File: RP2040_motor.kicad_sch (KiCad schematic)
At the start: 162 parts, among them J1 USB_C_Receptacle_USB2.0, J2 Conn_01x05, J3 Conn_01x06, J4 Conn_01x04, J5 Conn_01x04, J6 Conn_01x03, SW1 SW_MEC_5G, U1 EG2131, U10 EG2131, U11 RP2040, U2 EG2131, U3 LM358, U4 EG2131, U5 EG2131, U6 XL7045, U7 NCP1117-3.3_SOT223, U8 EG2131, U9 W25Q128JVS, Y1 Crystal_GND24

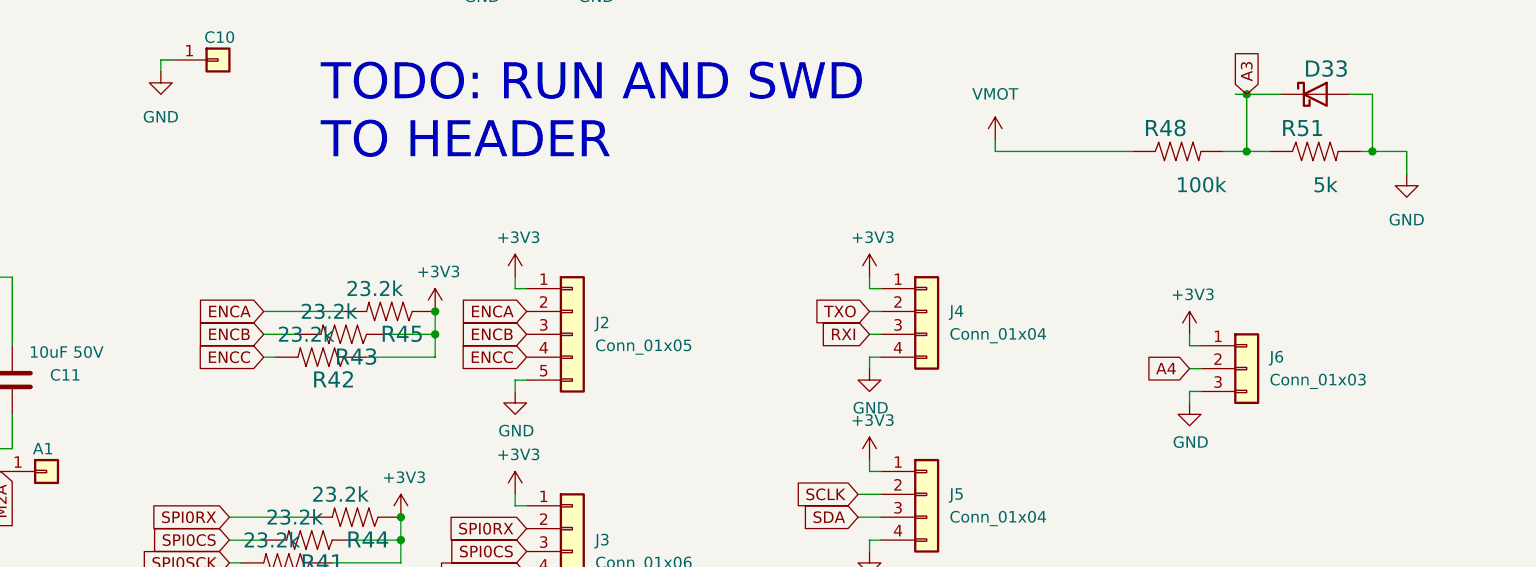
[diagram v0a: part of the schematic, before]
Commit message: Update files for price quote. DO NOT ORDER THESE BOARDS FROM THIS COMMIT!
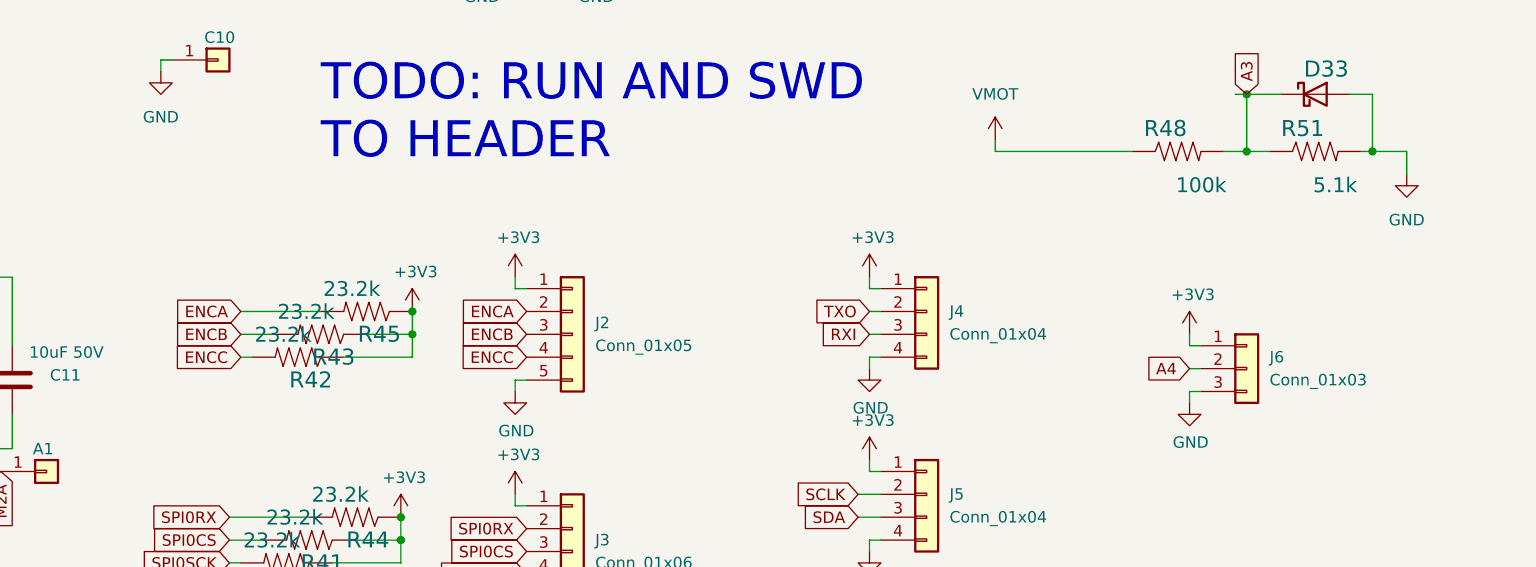
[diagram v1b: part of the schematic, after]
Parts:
- A1, A2, B1, B2, C10, C18, C5, C9: now left out of the parts list
- AH1, AH2, AL1, AL2, BH1, BH2, BL1, BL2, CH1, CH2, CL1, CL2: JLCPCB C180959 -> (none); LCSC (none) -> C180959
- C$1: JLCPCB C28233 -> (none); LCSC (none) -> C28233
- C$2: JLCPCB C440196 -> (none); LCSC (none) -> C440196
- C1, C12, C21, C25, C26, C29, C30, C32, C34, C35, C36, C37, C38, C39, C6, C8, R10, R31, R37: JLCPCB C14663 -> (none); LCSC (none) -> C14663
- C11, C17, C24, C28, C4, C7: JLCPCB C440198 -> (none); LCSC (none) -> C440198
- C13, C14, C15, C2, C3: JLCPCB C72524 -> (none); LCSC (none) -> C72524
- C16, C20, C27: JLCPCB C15850 -> (none); LCSC (none) -> C15850
- C19: JLCPCB C267470 -> (none); LCSC (none) -> C267470
- C22, C23: JLCPCB C1648 -> (none); LCSC (none) -> C1648
- C31, C33: JLCPCB C15849 -> (none); LCSC (none) -> C15849
- D1, D11, D16, D23, D28, D6: JLCPCB C511885 -> (none); LCSC (none) -> C511885
- D10, D14, D15, D19, D20, D21, D26, D27, D31, D32, D4, D5, D9: JLCPCB C8598 -> (none); LCSC (none) -> C8598
- D12, D13, D17, D18, D2, D24, D25, D29, D3, D30, D7, D8: JLCPCB C2128 -> (none); LCSC (none) -> C2128
- D22: JLCPCB C14996 -> (none); LCSC (none) -> C14996
- J1: JLCPCB C2835315 -> (none); LCSC (none) -> C2835315
- J2: JLCPCB C45012 -> (none); LCSC (none) -> C45012
- J3: JLCPCB C140771 -> (none); LCSC (none) -> C140771
- J4, J5: JLCPCB C402777 -> (none); LCSC (none) -> C402777
- J6: LCSC (none) -> C29275
- L1: JLCPCB C49622 -> (none); LCSC (none) -> C49622
- R1, R14, R15, R18, R19, R2, R28, R29, R38, R39, R7, R8: JLCPCB C23345 -> (none); LCSC (none) -> C23345
- R11, R33: JLCPCB C25977 -> (none); LCSC (none) -> C25977
- R12, R34: JLCPCB C403385 -> (none); LCSC (none) -> C403385
- R16, R17, R49, R50: JLCPCB C23186 -> (none); LCSC (none) -> C23186
- R20, R22, R24, R26, R3, R4, R5, R6: JLCPCB C469375 -> (none); LCSC (none) -> C469375
- R21: JLCPCB C37936 -> (none); LCSC (none) -> C37936
- R23: JLCPCB C13167 -> (none); LCSC (none) -> C13167
- R25, R40, R41, R42, R43, R44, R45: JLCPCB C23346 -> (none); LCSC (none) -> C23346
- R27, R30, R35, R9: JLCPCB C22764 -> (none); LCSC (none) -> C22764
- R46, R47: JLCPCB C25190 -> (none); LCSC (none) -> C25190
- R48: LCSC (none) -> C25803
- R51: value 5k -> 5.1k; LCSC (none) -> C23186
- SW1: JLCPCB C13828 -> (none); LCSC (none) -> C13828
- U$1: JLCPCB C21117 -> (none); LCSC (none) -> C21117
- U1, U10, U2, U4, U5, U8: JLCPCB C193777 -> (none); LCSC (none) -> C193777
- U11: JLCPCB C2040 -> (none); LCSC (none) -> C2040
- U3: LCSC (none) -> C7950
- U6: JLCPCB C126474 -> (none); LCSC (none) -> C126474
- U7: JLCPCB C6186 -> (none); LCSC (none) -> C6186
- U9: JLCPCB C97521 -> (none); LCSC (none) -> C97521
- Y1: JLCPCB C9002 -> (none); LCSC (none) -> C9002
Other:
- moved on the sheet: R42, R43, R45

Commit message: In progress independent phase current measurement.
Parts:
- removed R36: DNS, Resistor_SMD:R_0603_1608Metric, symbol MotorController:TAYLOR_RESISTOR
- added C40: 1u, Capacitor_SMD:C_0603_1608Metric, symbol Device:C
- added R36, R55, R58, R59: 0.1uF, Capacitor_SMD:C_0603_1608Metric, symbol MotorController:SPARKFUN-CAPACITORS_CAP
- added R52, R56: 4.64k, Resistor_SMD:R_0603_1608Metric, symbol MotorController:TAYLOR_RESISTOR
- added R53, R57: 133k, Resistor_SMD:R_0603_1608Metric, symbol MotorController:TAYLOR_RESISTOR
- added R54: 499R, Resistor_SMD:R_0603_1608Metric, symbol MotorController:TAYLOR_RESISTOR
- added U12: LM358, Package_SO:MSOP-8_3x3mm_P0.65mm, symbol Amplifier_Operational:LM358
- added U13: ADC081S021CISD/NOPB, ADC081S021:ADC081S021CISD&slash_NOPB, symbol 2022-06-16_01-48-54:ADC081S021CISD/NOPB
- R11, R33: value 6.04k -> 4.64k; LCSC C25977 -> C144652
- R12, R34: value 88.7K -> 133k; LCSC C403385 -> C423080
- R13: value DNS -> 499R; LCSC (none) -> C101076
- R20, R22, R24, R26, R3, R4, R5, R6: value 8mΩ -> 4mΩ; LCSC C469375 -> C375693
- R30, R9: value 1.1k -> 499R; LCSC C22764 -> C101076
- R31, R37: LCSC C14663 -> (none)
- U3: footprint Package_SO:SOIC-8_3.9x4.9mm_P1.27mm -> Package_SO:MSOP-8_3x3mm_P0.65mm; LCSC C7950 -> C54867
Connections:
- net GPIO23 is gone; now on net ENCC: U11.35 (GPIO23)
- net +3V3: now also C40.2, R58.1, R59.1, U12.8 (V+), U13.1 (VA); no longer J6.1 (Pin_1)
- net A1: now also R57.1, U12.1; no longer R34.1, U3.1
- net A2: now also R53.1, U12.7; no longer R12.1, R13.2, U3.7
- net A3: now also R34.1, U3.1; no longer D33.1 (K), R48.2, R51.1
- net A4: now also R12.1, U3.7; no longer J6.2 (Pin_2)
- net ENCC: no longer U11.34 (GPIO22)
- net GND: now also AL1.1 (S), CL2.1 (S), D15.2 (A), D21.2 (A), C40.1, R36.2, R52.2, R55.2, R56.2, R58.2, R59.2, U12.4 (V-), U13.2 (GND); no longer J6.3 (Pin_3), R13.1
- net RUN: now also J6.1 (Pin_1)
- net SWCLK: now also J6.2 (Pin_2)
- net SWD: now also J6.3 (Pin_3)
- net at R33.1, U3.2 (-): no longer R34.2
- net at R10.1, R9.2, U3.5 (+): now also R12.2
- net at R11.1, U3.6 (-): no longer R12.2
- net at R30.2, R31.1, U3.3 (+): now also R34.2
- net GPIO24 renamed ADC_DATA
- net ADC_DATA: now also U13.5 (SDATA)
- net GPIO25 renamed ADC_CS
- net ADC_CS: now also U13.6 (~{CS})
- removed net VSENSE1: AL2.1 (S), BL2.1 (S), CL2.1 (S), D21.2 (A), D27.2 (A), D32.2 (A), R20.2, R22.2, R24.2, R26.2, R30.1
- removed net VSENSE2: AL1.1 (S), BL1.1 (S), CL1.1 (S), D10.2 (A), D15.2 (A), D5.2 (A), R3.2, R4.2, R5.2, R6.2, R9.1
- new net: D33.1 (K), R48.2, R51.1, U13.3 (VIN)
- new net: R13.2, R36.1, R53.2, U12.5 (+)
- new net: R52.1, U12.6 (-)
- new net: R56.1, U12.2 (-)
- new net: R54.2, R55.1, R57.2, U12.3 (+)
- new net ADC_CLK: U11.34 (GPIO22), U13.4 (SCLK)
- new net VSENSE1A: AL2.1 (S), D32.2 (A), R22.2, R24.2, R30.1
- new net VSENSE1B: BL2.1 (S), D27.2 (A), R20.2, R26.2, R9.1
- new net VSENSE2B: BL1.1 (S), D10.2 (A), R13.1, R3.2, R4.2
- new net VSENSE2C: CL1.1 (S), D5.2 (A), R5.2, R54.1, R6.2
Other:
- note added: "55A Max"
- note removed: "TODO: RUN AND SWD TO HEADER"
- moved on the sheet: C13, C14, C15, D33, J6, R10, R11, R12, R20, R22, R24, R26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

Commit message: Break out to two page schematic. Update images and schematic PDF
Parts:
- removed A1, A2, B1, B2, C18, C5: HIGHCURRENTPAD2, RP2040_minimal:PAD_12GA_WIRE, symbol Connector_Generic:Conn_01x01
- removed AH1, AH2, AL1, AL2, BH1, BH2, BL1, BL2, CH1, CH2, CL1, CL2: MOSFETSO-8, motor:PowerPAK_SO-8_123, symbol Device:Q_NMOS_SGD
- removed C$1: 100nF 100V, Capacitor_SMD:C_0805_2012Metric, symbol Device:C
- removed C$2: 1uF 35V, Capacitor_SMD:C_0805_2012Metric, symbol Device:C
- removed C1, C12, C21, C26, C6, C8: 100nF 50V, Capacitor_SMD:C_0603_1608Metric, symbol Device:C
- removed C10, C9: HIGHCURRENTPAD2, RP2040_minimal:PAD_8GA_WIRE, symbol Connector_Generic:Conn_01x01
- removed C11, C17, C24, C28, C4, C7: 10uF 50V, Capacitor_SMD:C_0805_2012Metric, symbol Device:C
- removed C13, C14, C15, C2, C3: 47uF 63V, Capacitor_SMD:CP_Elec_8x10, symbol Device:C_Polarized
- removed C16, C20, C27: 10u, Capacitor_SMD:C_0805_2012Metric, symbol Device:C
- removed C19: 100uF 35V, Capacitor_SMD:CP_Elec_6.3x7.7, symbol Device:C_Polarized
- removed C22, C23: 20p, Capacitor_SMD:C_0603_1608Metric, symbol Device:C
- removed C25, C29, C30, C32, C34, C35, C36, C37, C38, C39: 100n, Capacitor_SMD:C_0603_1608Metric, symbol Device:C
- removed C31, C33, C40: 1u, Capacitor_SMD:C_0603_1608Metric, symbol Device:C
- removed D1, D11, D16, D23, D28, D6: FR107, Diode_SMD:D_SOD-123, symbol Device:D
- removed D10, D14, D15, D19, D20, D21, D26, D27, D31, D32, D4, D5, D9: B5819W SL, Diode_SMD:D_SOD-123, symbol Diode:MBR340
- removed D12, D13, D17, D18, D2, D24, D25, D29, D3, D30, D7, D8: 1N4148WS, Diode_SMD:D_SOD-323, symbol Device:D
- removed D22: SS210, Diode_SMD:D_SMA, symbol Diode:MBR340
- removed D33: DNS, Diode_SMD:D_SOD-523, symbol Diode:MBR340
- removed J1: USB_C_Receptacle_USB2.0, Connector_USB:USB_C_Receptacle_XKB_U262-16XN-4BVC11, symbol Connector:USB_C_Receptacle_USB2.0
- removed J2: Conn_01x05, Connector_Molex:Molex_KK-254_AE-6410-05A_1x05_P2.54mm_Vertical, symbol Connector_Generic:Conn_01x05
- removed J3: Conn_01x06, Connector_Molex:Molex_KK-254_AE-6410-06A_1x06_P2.54mm_Vertical, symbol Connector_Generic:Conn_01x06
- removed J4, J5: Conn_01x04, Connector_Molex:Molex_KK-254_AE-6410-04A_1x04_P2.54mm_Vertical, symbol Connector_Generic:Conn_01x04
- removed J6: Conn_01x03, Connector_Molex:Molex_KK-254_AE-6410-03A_1x03_P2.54mm_Vertical, symbol Connector_Generic:Conn_01x03
- removed L1: 100uH 0.5A, RP2040_minimal:SM5845, symbol Device:L
- removed R1, R14, R15, R18, R19, R2, R28, R29, R38, R39, R7, R8: 22R, Resistor_SMD:R_0603_1608Metric, symbol MotorController:TAYLOR_RESISTOR
- removed R10, R31, R36, R37, R55, R58, R59: 0.1uF, Capacitor_SMD:C_0603_1608Metric, symbol MotorController:SPARKFUN-CAPACITORS_CAP
- removed R11, R33, R52, R56: 4.64k, Resistor_SMD:R_0603_1608Metric, symbol MotorController:TAYLOR_RESISTOR
- removed R12, R34, R53, R57: 133k, Resistor_SMD:R_0603_1608Metric, symbol MotorController:TAYLOR_RESISTOR
- removed R13, R30, R54, R9: 499R, Resistor_SMD:R_0603_1608Metric, symbol MotorController:TAYLOR_RESISTOR
- removed R16, R17, R49, R50: 5.1k, Resistor_SMD:R_0603_1608Metric, symbol Device:R
- removed R20, R22, R24, R26, R3, R4, R5, R6: 4mΩ, Resistor_SMD:R_2512_6332Metric, symbol MotorController:TAYLOR_RESISTOR
- removed R21: 0.15R, Resistor_SMD:R_1206_3216Metric, symbol MotorController:TAYLOR_RESISTOR
- removed R23: 2.7k, Resistor_SMD:R_0603_1608Metric, symbol MotorController:TAYLOR_RESISTOR
- removed R25, R40, R41, R42, R43, R44, R45: 23.2k, Resistor_SMD:R_0603_1608Metric, symbol MotorController:TAYLOR_RESISTOR
- removed R27, R35: 1.1k, Resistor_SMD:R_0603_1608Metric, symbol Device:R
- removed R32: DNS, Capacitor_SMD:C_0402_1005Metric, symbol Device:R
- removed R46, R47: 27, Resistor_SMD:R_0603_1608Metric, symbol Device:R
- removed R48: 100k, Resistor_SMD:R_0603_1608Metric, symbol MotorController:TAYLOR_RESISTOR
- removed R51: 5.1k, Resistor_SMD:R_0603_1608Metric, symbol MotorController:TAYLOR_RESISTOR
- removed SW1: SW_MEC_5G, Button_Switch_THT:SW_PUSH_6mm_H4.3mm, symbol Switch:SW_Push
- removed U$1: 33Nf, Capacitor_SMD:C_0603_1608Metric, symbol Device:C
- removed U1, U10, U2, U4, U5, U8: EG2131, Package_SO:SOIC-8_3.9x4.9mm_P1.27mm, symbol MotorBuck:EG2131
- removed U11: RP2040, RP2040_minimal:RP2040-QFN-56, symbol MCU_RaspberryPi_RP2040:RP2040
- removed U12, U3: LM358, Package_SO:MSOP-8_3x3mm_P0.65mm, symbol Amplifier_Operational:LM358
- removed U13: ADC081S021CISD/NOPB, ADC081S021:ADC081S021CISD&slash_NOPB, symbol 2022-06-16_01-48-54:ADC081S021CISD/NOPB
- removed U6: XL7045, RP2040_minimal:SOIC-8_3.9x4.9mm_P1.27mm_POWERPAD, symbol MotorBuck:XL7045
- removed U7: NCP1117-3.3_SOT223, Package_TO_SOT_SMD:SOT-223-3_TabPin2, symbol Regulator_Linear:NCP1117-3.3_SOT223
- removed U9: W25Q128JVS, Package_SO:SOIC-8_5.23x5.23mm_P1.27mm, symbol Memory_Flash:W25Q128JVS
- removed Y1: Crystal_GND24, Crystal:Crystal_SMD_3225-4Pin_3.2x2.5mm, symbol Device:Crystal_GND24
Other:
- added sheet gate_drive (gate_drive.kicad_sch)
- added sheet power_and_cpu (power_and_cpu.kicad_sch)
- note removed: "55A Max"
- note removed: "Crystal"
- note removed: "Flash"
- note removed: "IOs"
- note removed: "Make sure C10 is close to pin 44 of RP2040"
- note removed: "Make sure C8 is close to pin 45 of RP2040"
- note removed: "Make sure R4 and R5 are close to RP2040"
- note removed: "Power"
